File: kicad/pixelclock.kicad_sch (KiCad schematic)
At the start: 21 parts, among them J1 UART/ISP, J2 LED, J3 USB_B_Micro, J4 5V, J5 LED, Q1 BC848, Q2 BC848, SW1 Reset, U1 ESP32-WROOM-32, U2 SN74LV1T34DBV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

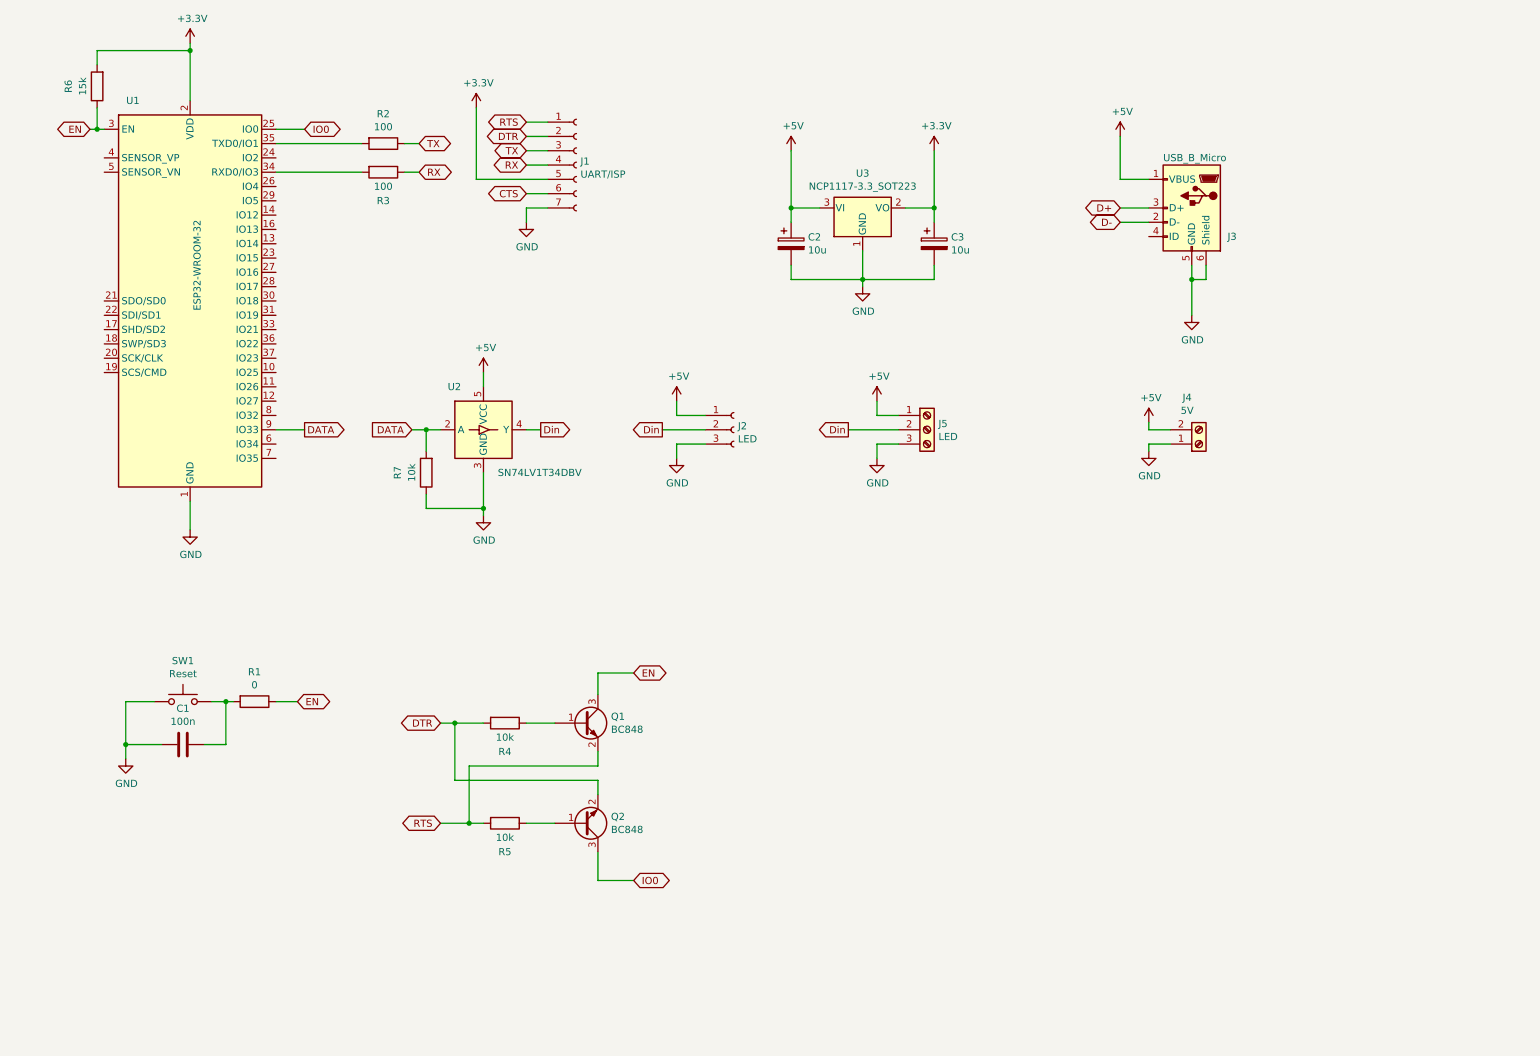
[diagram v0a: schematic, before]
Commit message: Update pixelclock board to support additional RGBW LED strip (dumb single color LED strip)
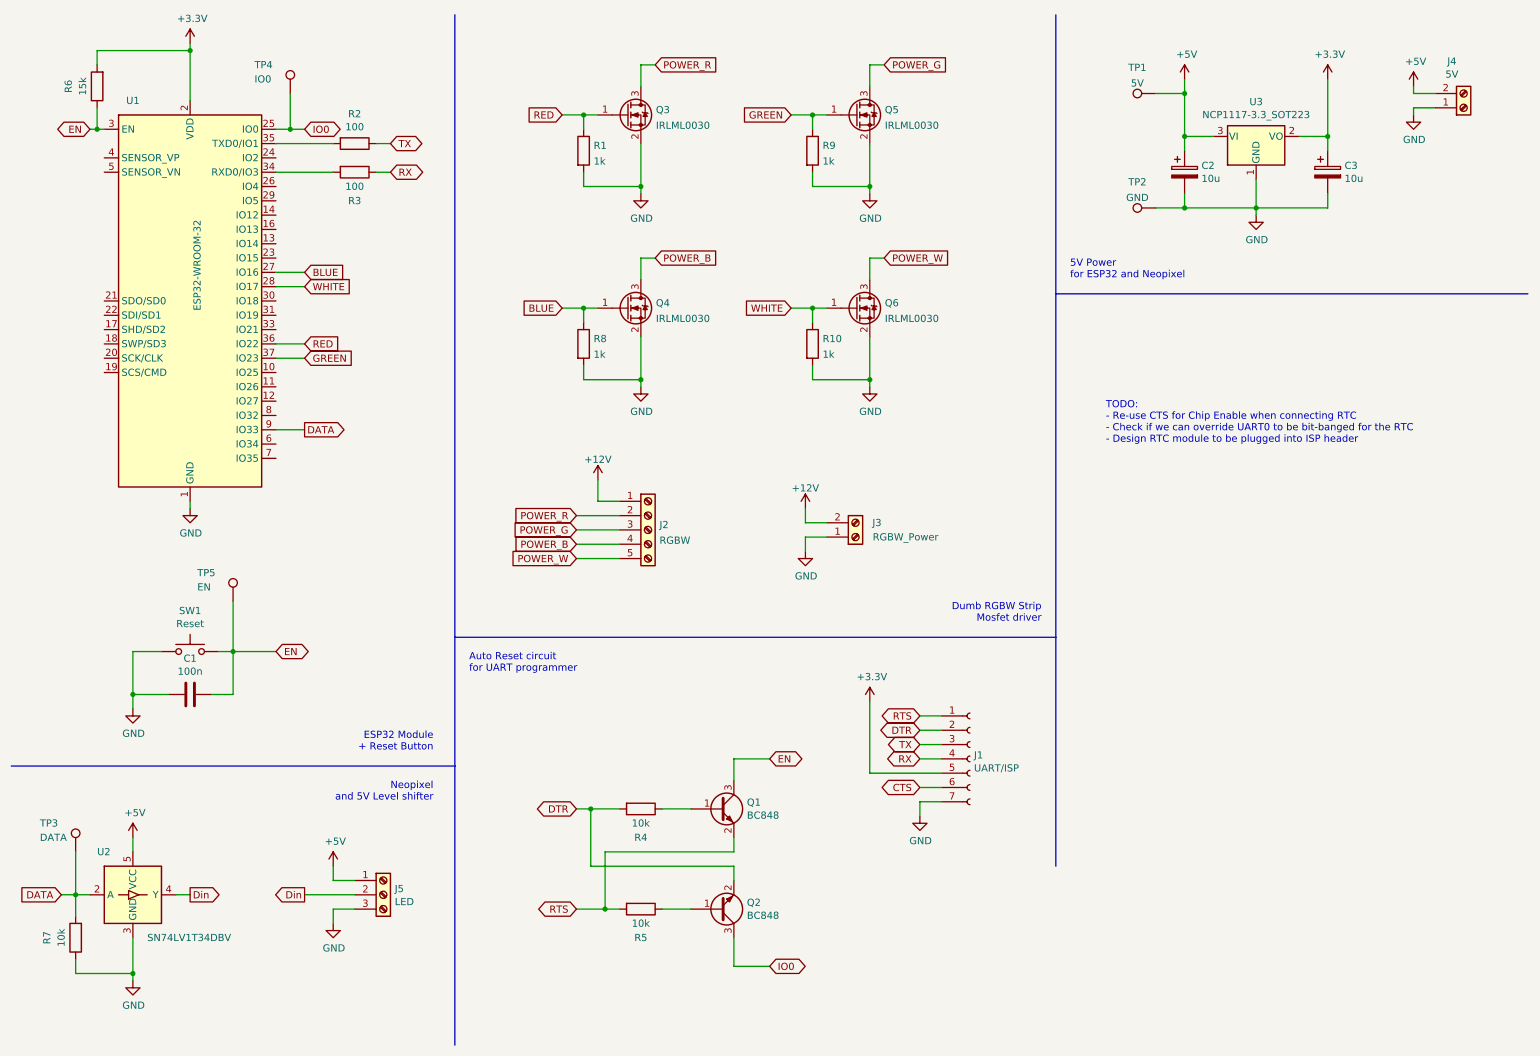
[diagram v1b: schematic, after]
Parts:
- removed J2: LED, Connector_PinSocket_2.54mm:PinSocket_1x03_P2.54mm_Vertical, symbol Connector:Conn_01x03_Female
- removed J3: USB_B_Micro, Connector_USB:USB_Micro-B_Amphenol_10104110_Horizontal, symbol Connector:USB_B_Micro
- added J2: RGBW, TerminalBlock_Phoenix:TerminalBlock_Phoenix_PT-1,5-5-3.5-H_1x05_P3.50mm_Horizontal, symbol Connector:Screw_Terminal_01x05
- added J3: RGBW_Power, TerminalBlock_Phoenix:TerminalBlock_Phoenix_PT-1,5-2-3.5-H_1x02_P3.50mm_Horizontal, symbol Connector:Screw_Terminal_01x02
- added Q3, Q4, Q5, Q6: IRLML0030, Package_TO_SOT_SMD:SOT-23, symbol Transistor_FET:IRLML0030
- added R10, R8, R9: 1k, Resistor_SMD:R_0805_2012Metric_Pad1.20x1.40mm_HandSolder, symbol Device:R
- added TP1: 5V, TestPoint:TestPoint_Pad_1.5x1.5mm, symbol Connector:TestPoint
- added TP2: GND, TestPoint:TestPoint_Pad_1.5x1.5mm, symbol Connector:TestPoint
- added TP3: DATA, TestPoint:TestPoint_Pad_1.5x1.5mm, symbol Connector:TestPoint
- added TP4: IO0, TestPoint:TestPoint_Pad_1.5x1.5mm, symbol Connector:TestPoint
- added TP5: EN, TestPoint:TestPoint_Pad_1.5x1.5mm, symbol Connector:TestPoint
- J4: footprint TerminalBlock_Phoenix:TerminalBlock_Phoenix_PT-1,5-2-5.0-H_1x02_P5.00mm_Horizontal -> TerminalBlock_Phoenix:TerminalBlock_Phoenix_PT-1,5-2-3.5-H_1x02_P3.50mm_Horizontal
- R1: value 0 -> 1k; footprint Resistor_SMD:R_1206_3216Metric_Pad1.30x1.75mm_HandSolder -> Resistor_SMD:R_0805_2012Metric_Pad1.20x1.40mm_HandSolder
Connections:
- net +5V: now also TP1.1
- net DATA: now also TP3.1
- net EN: now also C1.1, SW1.2, TP5.1; no longer R1.1
- net GND: now also R1.2, J3.1 (Pin_1), Q3.2 (S), Q4.2 (S), Q5.2 (S), Q6.2 (S), R10.2, R8.2, R9.2, TP2.1
- net IO0: now also TP4.1
- net BLUE: now reaches U1.27 (IO16)
- net BLUE: now also Q4.1 (G), R8.1
- net WHITE: now reaches U1.28 (IO17)
- net WHITE: now also Q6.1 (G), R10.1
- net RED: now reaches U1.36 (IO22)
- net RED: now also R1.1, Q3.1 (G)
- net GREEN: now reaches U1.37 (IO23)
- net GREEN: now also Q5.1 (G), R9.1
- new net +12V: J2.1 (Pin_1), J3.2 (Pin_2)
- new net POWER_B: J2.4 (Pin_4), Q4.3 (D)
- new net POWER_G: J2.3 (Pin_3), Q5.3 (D)
- new net POWER_R: J2.2 (Pin_2), Q3.3 (D)
- new net POWER_W: J2.5 (Pin_5), Q6.3 (D)
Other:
- note added: "5V Power for ESP32 and Neopixel"
- note added: "Auto Reset circuit for UART programmer"
- note added: "Dumb RGBW Strip Mosfet driver"
- note added: "ESP32 Module + Reset Button"
- note added: "Neopixel and 5V Level shifter"
- note added: "TODO: - Re-use CTS for Chip Enable when connecting RTC - Check if we can override UART0 to be bit-banged for the RTC - Design RTC module to be plugged into ISP header"
- moved on the sheet: C1, C2, C3, J1, J4, J5, Q1, Q2, R2, R3, R4, R5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
